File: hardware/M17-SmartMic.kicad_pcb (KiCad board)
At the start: 4 copper layers, 84.9 x 89.9 mm, 182 parts, among them IC1 LM4861M, J1 Kenwood-2.5, J10 UART, J11 Radio_Opt, J12 Speaker, J2 USB_C, J3 OLED, J4 CAT_TX, J5 Kenwood-3.5, J6 CAT_TX, J7 Radio, J8 +12V, J9 STLink, Q1 IRLML2060, Q2 BSS138, Q3 BSS138, Q4 IRLML2244, Q5 MMBT3904, SW1 Button Up, SW2 Button Down, SW3 Reset, SW4 Button Escape, SW5 Button Left, SW6 Button Enter, SW7 Button Right, SW8 Button Power, U1 MAX9814, U10 STM32F405RGTx, U11 TPS7A2033, U2 TP6841S6, U3 USBLC6-2, U6 MCP6002, U7 MCP6002, Y1 8 MHz

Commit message: Started new PCB layout
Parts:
- removed C10: 1n, pkl_dipol:C_0603
- removed R2: 22k, pkl_dipol:R_0603
- added C201: 10n, pkl_dipol:C_0603, F.Cu at (126.8, 121.5)
- added C202: 4.7n, pkl_dipol:C_0603, F.Cu at (116.6, 123.2)
- added C203: 100n, pkl_dipol:C_0603, F.Cu at (121.0, 121.8)
- added C513: 100n, pkl_dipol:C_0603, F.Cu at (151.5, 68.9)
- added C514: 100n, pkl_dipol:C_0603, F.Cu at (132.3, 68.6)
- added R201: 7.5k, pkl_dipol:R_0603, F.Cu at (123.0, 125.8)
- added R202: 4.7k, pkl_dipol:R_0603, F.Cu at (123.7, 123.2)
- added R69: 0, pkl_dipol:R_0603, F.Cu at (106.0, 134.5)
- added R70: 0, pkl_dipol:R_0603, F.Cu at (106.0, 136.8)
- added U201: MCP6002, Package_SO:SOIC-8_3.9x4.9mm_P1.27mm, F.Cu at (132.9, 123.1)
- added U503: MCP4551, Package_SO:MSOP-8_3x3mm_P0.65mm, F.Cu at (135.1, 71.5)
- added U504: MCP4551, Package_SO:MSOP-8_3x3mm_P0.65mm, F.Cu at (154.2, 70.7)
- IC1: value LM4861M -> LM4991xx
- RV2, RV3: footprint Potentiometer_SMD:Potentiometer_Bourns_3224W_Vertical -> Potentiometer_SMD:Potentiometer_Bourns_3224J_Horizontal
- moved Ref** 179.8 mm to (28.6, 40.9)
- moved Ref** 177.8 mm to (30.9, 25.3)
- moved REF** 172.6 mm to (25.7, 56.8)
- moved REF** 172.6 mm to (25.7, 55.9)
- moved J9 123.3 mm to (65.8, 84.5), turned to 180 degrees
- moved R50 122.7 mm to (69.2, 79.8), turned to 180 degrees
- moved R3 121.3 mm to (69.2, 81.2), turned to 180 degrees
- moved R4 119.9 mm to (69.2, 82.6), turned to 180 degrees
- moved Q1 114.8 mm to (106.4, 122.8), turned to 0 degrees
- moved C54 111.1 mm to (109.0, 122.8), turned to 90 degrees
- moved R49 108.2 mm to (111.1, 122.0), turned to 180 degrees
- moved R51 108.1 mm to (111.1, 123.5), turned to 0 degrees
- moved TP6 108.0 mm to (76.8, 120.2)
- moved J6 106.8 mm to (96.1, 109.8), turned to 90 degrees
- moved J4 104.6 mm to (97.7, 109.8), turned to 90 degrees
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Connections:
- net /Microcontroller/xUDN renamed /Connectors/xUDN
- net /Microcontroller/xUDP renamed /Connectors/xUDP
- net Net-(R41-Pad2) renamed /Baseband/BB_RX_A
- net Net-(R42-Pad1) renamed /Baseband/BB_RX_B
- net Net-(U6A-+) renamed /Baseband/BB_TX_W
- net Net-(U7A--) renamed /Baseband/BB_RX_W
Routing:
- net +5V: track 197.6 -> 20.9 mm, vias 6 -> 1
- net VDD: track 94.8 -> 0.00 mm, vias 19 -> 2
- net BTN_RIGHT: track 77.7 -> 0.00 mm, vias 2 -> 0
- net BTN_DOWN: track 76.7 -> 0.00 mm, vias 2 -> 0
- net BTN_LEFT: track 65.2 -> 0.00 mm, vias 2 -> 0
- net BTN_ENT: track 65.1 -> 0.00 mm, vias 2 -> 0
- net ~{BOOT0}: track 59.6 -> 0.00 mm, vias 2 -> 0
- net BTN_UP: track 59.0 -> 0.00 mm, vias 2 -> 0
- net LED-ERROR: track 50.4 -> 0.00 mm, vias 2 -> 0
- net LED-SYNC: track 50.0 -> 0.00 mm, vias 2 -> 0
- net LED-PTT: track 49.6 -> 0.00 mm, vias 2 -> 0
- net VIN: track 79.3 -> 31.6 mm
- net GPIO_POWER: track 47.7 -> 1.62 mm, vias 2 -> 1
- net NRST: track 45.1 -> 0.00 mm, vias 1 -> 0
- net OLED_SPI_MOSI: track 40.6 -> 0.00 mm, vias 1 -> 0
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- removed copper zone on B.Cu, net GND
- removed copper zone on F.Cu, net GND
- removed copper zone on In2.Cu, net GND
- removed copper zone on In1.Cu, net VDD
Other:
- board size 84.9 x 89.9 mm -> 100 x 80 mm
- board text added: "OHIS 8P8C"
- board text added: "TP_BBRX"
- board text added: "TP_BBTX"
- board text removed: "SPK_PRE"

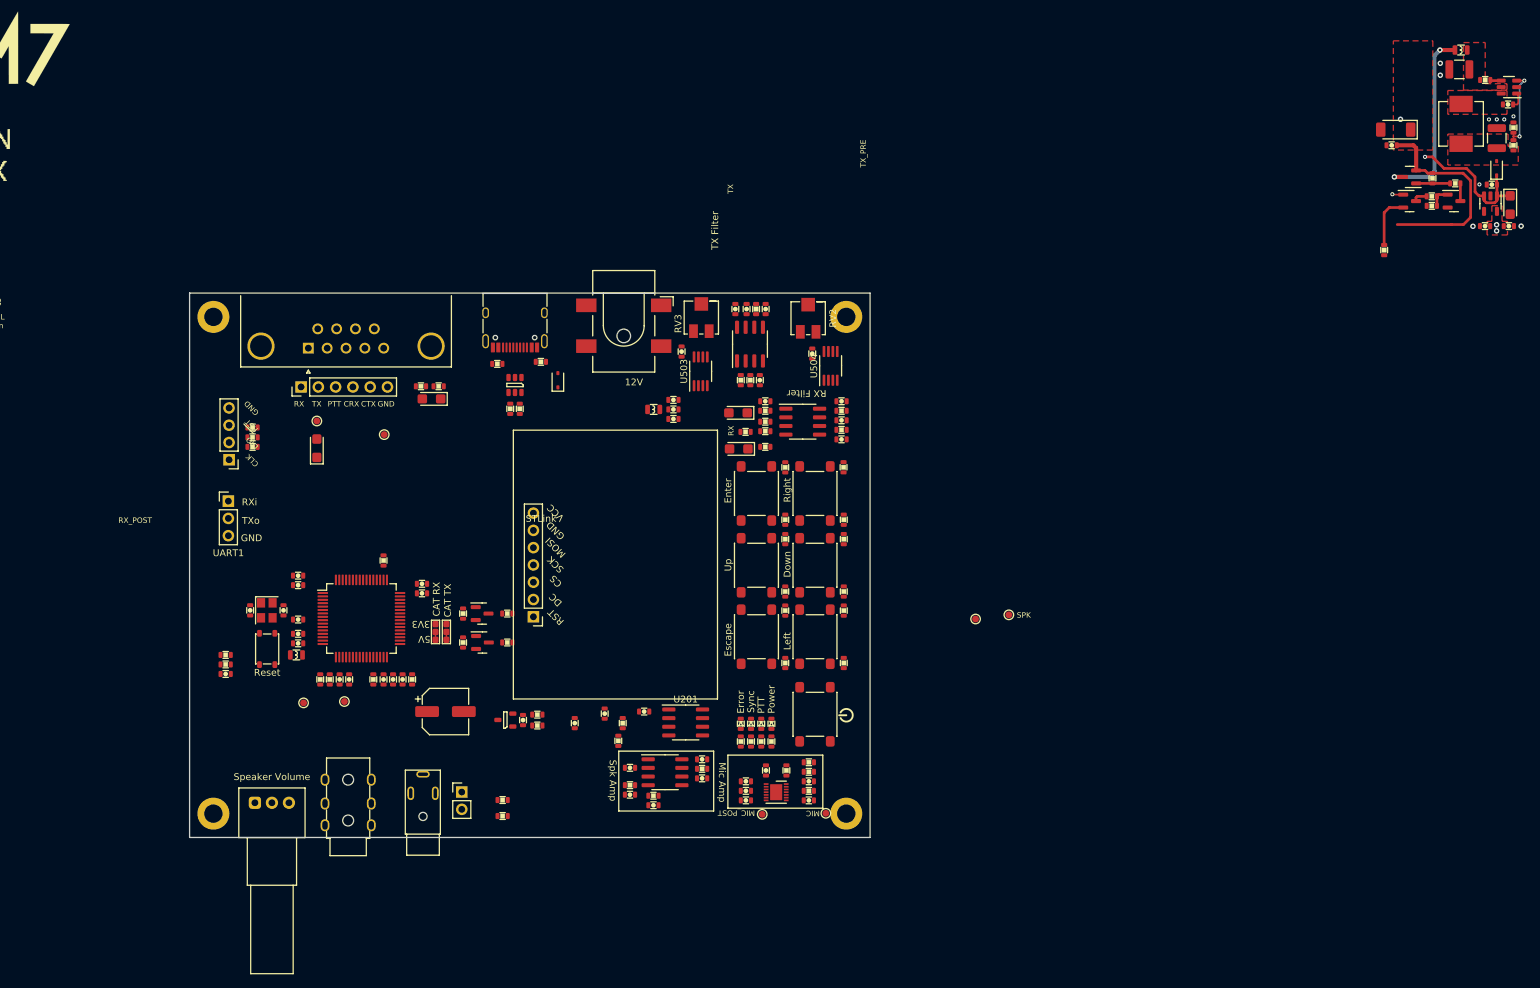
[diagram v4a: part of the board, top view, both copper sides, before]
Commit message: [WIP] PCB layout and routing
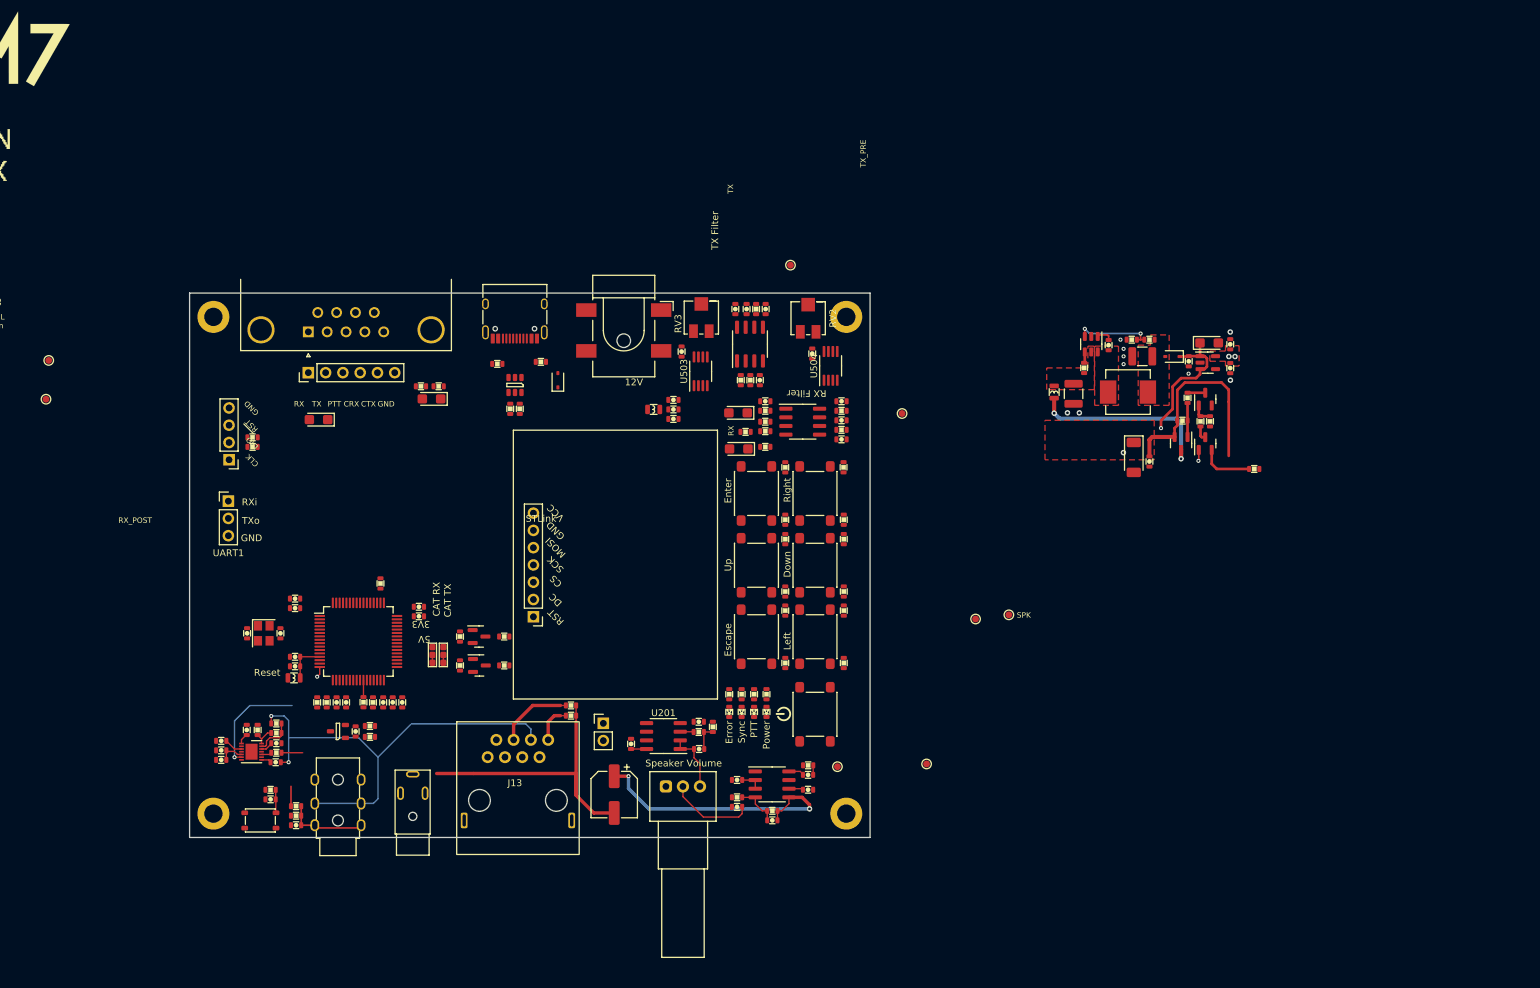
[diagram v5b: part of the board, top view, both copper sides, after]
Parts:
- added J13: KH-RJ45-58-8P8C, M17-SmartMic:KH-RJ45-58-8P8C, F.Cu at (108.2, 142.5)
- moved TP6 97.7 mm to (164.7, 77.7)
- moved TP5 91.7 mm to (148.3, 55.9)
- moved R1 78.6 mm to (72.8, 123.2), turned to 180 degrees
- moved C9 78.5 mm to (72.7, 128.9)
- moved C21 78.5 mm to (72.8, 126.2)
- moved R8 78.5 mm to (72.8, 127.5)
- moved R30 78.4 mm to (72.8, 124.7), turned to 0 degrees
- moved FB2 78.1 mm to (187.1, 74.5), turned to -90 degrees
- moved R23 77.9 mm to (70.0, 124.2)
- moved C29 77.3 mm to (64.7, 125.8)
- moved C46 77.3 mm to (64.7, 128.6)
- moved C47 77.3 mm to (64.7, 127.2)
- moved U1 77.3 mm to (69.1, 127.4)
- moved C12 76.5 mm to (68.4, 124.2)
- moved C62 74.1 mm to (189.9, 74.8), turned to -90 degrees
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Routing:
- net MIC: track 0.00 -> 67.5 mm, vias 0 -> 2
- net SPEAKER: track 0.14 -> 43.7 mm
- net Net-(IC1-VO1): track 0.00 -> 40.3 mm, vias 0 -> 2
- net AUDIO_MIC: track 0.00 -> 17.3 mm, vias 0 -> 2
- net Net-(C20-Pad1): track 0.00 -> 12.6 mm
- net Net-(C32-Pad1): track 0.00 -> 11.9 mm
- net Net-(J13-Pad4): track 0.00 -> 11.0 mm
- net Net-(U201A--): track 0.00 -> 9.16 mm
- net Net-(IC1--IN): track 0.00 -> 6.48 mm
- net VDDA: track 0.00 -> 5.97 mm
- net Net-(U1-MICBIAS): track 0.00 -> 5.73 mm
- net Net-(J13-Pad8): track 0.00 -> 5.53 mm
- net VDD: track 0.00 -> 3.87 mm
- net Net-(C201-Pad1): track 0.00 -> 3.72 mm
- net Net-(U1-TH): track 0.00 -> 3.28 mm
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- added copper zone on In1.Cu, net GND
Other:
- board text added: "Volume knob sticks out of the board by : 1.6mm (PCB thickness for enclosure) + 2mm (nut thickness) + 0.5mm (washer thickness) + 0.4mm (tolerance margin) = 4.5mm"
- board text removed: "MIC"
- board text removed: "MIC_POST"
- board text removed: "Mic Amp"
- board text removed: "OHIS 8P8C"
- board text removed: "Spk Amp"

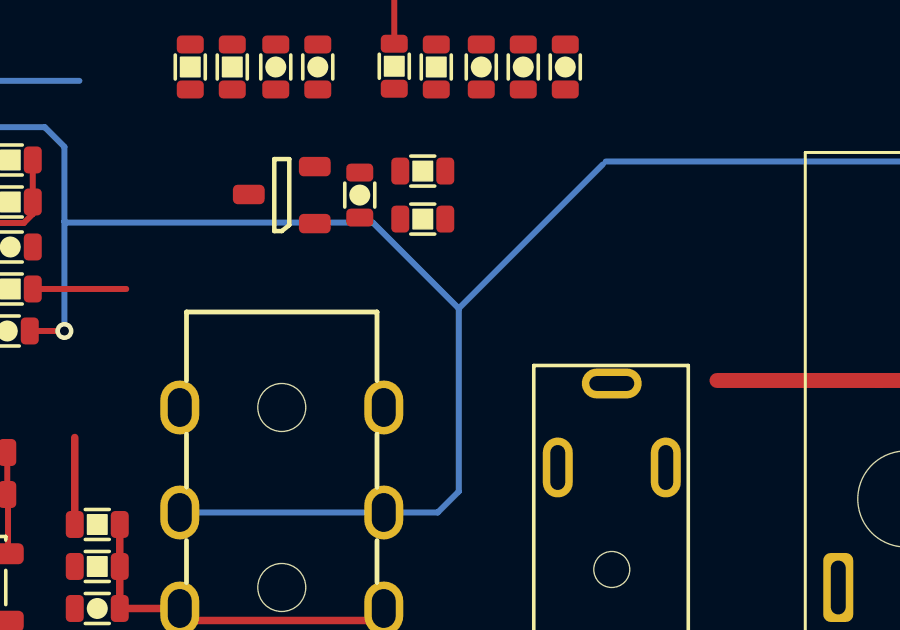
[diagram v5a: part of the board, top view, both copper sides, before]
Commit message: Switched to M17_kicad_library for custom symbols/footprints
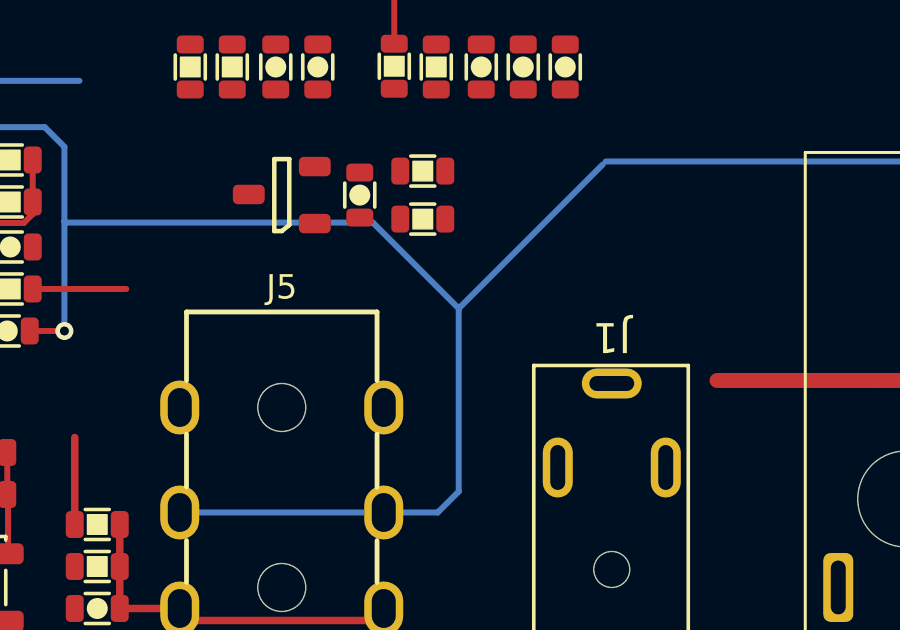
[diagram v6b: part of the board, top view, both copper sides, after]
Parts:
- J1: footprint M17-SmartMic:PJ-211A -> M17_connectors:PJ-211A
- J13: footprint M17-SmartMic:KH-RJ45-58-8P8C -> M17_connectors:KH-RJ45-58-8P8C
- J5: footprint M17-SmartMic:PJ-3136-B -> M17_connectors:PJ-3136-B
- U503: value MCP4551 -> MCP4551-103
- U504: value MCP4551 -> MCP455x
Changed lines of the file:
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@@
   (net 147 "Net-(J2-CC2)")
   (net 148 "Net-(J2-CC1)")
-  (footprint "M17-SmartMic:KH-RJ45-58-8P8C" (layer "F.Cu")
+  (footprint "M17_connectors:KH-RJ45-58-8P8C" (layer "F.Cu")
     (at 108.25 142.5)
     (property "LCSC Part #" "C2683360")
@@
       (net 45 "RADIO_TX") (pinfunction "1") (pintype "passive"))
   )
-  (footprint "M17-SmartMic:PJ-211A" (layer "F.Cu")
+  (footprint "M17_connectors:PJ-211A" (layer "F.Cu")
     (at 92.8 136.9 90)
     (property "LCSC Part #" "C480265")
@@
     (property "ki_keywords" "audio jack receptacle stereo headphones phones TRS connector")
     (attr through_hole)
-    (fp_text reference "J1" (at 7.75 0 180 unlocked) (layer "F.Fab")
+    (fp_text reference "J1" (at 7.75 0 180 unlocked) (layer "F.SilkS")
         (effects (font (size 1 1) (thickness 0.15)))
     )
@@
     (descr "SOIC, 8 Pin (JEDEC MS-012AA, https://www.analog.com/media/en/package-pcb-resources/package/pkg_pdf/soic_narrow-r/r_8.pdf), generated with kicad-footprint-generator ipc_gullwing_generator.py")
     (tags "SOIC SO")
-    (property "Description" "TEXAS INSTRUMENTS - LM4991xx - Audio Power Amplifier, 3 W, AB, 1 Channel, 2V to 5.5V, 8 Pins")
+    (property "LCSC Part #" "C2860134")
+    (property "MPN" "LM4991MA/NOPB")
     (property "Sheetfile" "Audio.kicad_sch")
     (property "Sheetname" "Audio & Filter")
     (property "ki_description" "TEXAS INSTRUMENTS - LM4991 - Audio Power Amplifier, 3 W, AB, 1 Channel, 2V to 5.5V, 8 Pins")
+    (property "ki_keywords" "Audio Amplifier shutdown")
     (attr smd)
     (fp_text reference "IC1" (at 0.035 -0.015) (layer "F.Fab")
@@
     (descr "MSOP, 8 Pin (https://www.jedec.org/system/files/docs/mo-187F.pdf variant AA), generated with kicad-footprint-generator ipc_gullwing_generator.py")
     (tags "MSOP SO")
+    (property "LCSC Part #" "C636116")
+    (property "MPN" "MCP4551-103E/MS")
     (property "Sheetfile" "baseband.kicad_sch")
     (property "Sheetname" "Baseband")
+    (property "ki_description" "7/8-Bit Single/Dual I2C Digital POT with Volatile Memory")
+    (property "ki_keywords" "digital potentiometer")
     (attr smd)
     (fp_text reference "U503" (at 0 -2.45 90) (layer "F.SilkS")
         (effects (font (size 1 1) (thickness 0.15)))
     )
-    (fp_text value "MCP4551" (at 0 2.45 90) (layer "F.Fab")
+    (fp_text value "MCP4551-103" (at 0 2.45 90) (layer "F.Fab")
         (effects (font (size 1 1) (thickness 0.15)))
     )
@@
     )
   )
-  (footprint "M17-SmartMic:PJ-3136-B" (layer "F.Cu")
+  (footprint "M17_connectors:PJ-3136-B" (layer "F.Cu")
     (at 81.8 140 90)
     (property "LCSC Part #" "C381131")
@@
     (property "ki_keywords" "audio jack receptacle stereo headphones phones TRS connector")
     (attr through_hole)
-    (fp_text reference "J5" (at 12.5095 0) (layer "F.Fab")
+    (fp_text reference "J5" (at 12.5095 0 180) (layer "F.SilkS")
         (effects (font (size 0.8128 0.8128) (thickness 0.1524)))
     )
@@
         (effects (font (size 0.8128 0.8128) (thickness 0.1524)))
     )
-    (fp_text user "${REFERENCE}" (at 12.5095 0) (layer "B.Fab")
+    (fp_text user "${REFERENCE}" (at 12.5095 0 180) (layer "B.SilkS")
         (effects (font (size 0.8128 0.8128) (thickness 0.1524)) (justify mirror))
     )
@@
     (descr "MSOP, 8 Pin (https://www.jedec.org/system/files/docs/mo-187F.pdf variant AA), generated with kicad-footprint-generator ipc_gullwing_generator.py")
     (tags "MSOP SO")
+    (property "LCSC Part #" "C636116")
+    (property "MPN" "MCP4551-103E/MS")
     (property "Sheetfile" "baseband.kicad_sch")
     (property "Sheetname" "Baseband")
+    (property "ki_description" "7/8-Bit Single/Dual I2C Digital POT with Volatile Memory")
+    (property "ki_keywords" "digital potentiometer")
     (attr smd)
     (fp_text reference "U504" (at 0 -2.45 90) (layer "F.SilkS")
         (effects (font (size 1 1) (thickness 0.15)))
     )
-    (fp_text value "MCP4551" (at 0 2.45 90) (layer "F.Fab")
+    (fp_text value "MCP455x" (at 0 2.45 90) (layer "F.Fab")
         (effects (font (size 1 1) (thickness 0.15)))
     )
@@
     (property "Sheetfile" "Microcontroller.kicad_sch")
     (property "Sheetname" "Microcontroller")
+    (property "ki_description" "40V 0.8A 800kHz Synchronous Step-Down Converter")
+    (property "ki_keywords" "buck converter step-down")
     (attr smd)
     (fp_text reference "U2" (at 0 -2.4 -270) (layer "F.Fab")

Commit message: Synchronized PCB and schematic
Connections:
- FB1 pad 1: VDDA -> VDD
- FB1 pad 2: VDD -> VDDA
- U10 pad 55: SPI1_SCK -> unconnected-(U10-PB3-Pad55)
- U10 pad 56: SPI1_MISO -> unconnected-(U10-PB4-Pad56)
- U10 pad 57: SPI1_MOSI -> unconnected-(U10-PB5-Pad57)
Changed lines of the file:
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@@
   (net 64 "BTN_RIGHT")
   (net 65 "GPIO_POWER")
-  (net 66 "SPI1_SCK")
+  (net 66 "unconnected-(U10-PB3-Pad55)")
   (net 67 "LED-PTT")
   (net 68 "LED-SYNC")
@@
   (net 111 "Net-(U2-EN)")
   (net 112 "VBAT")
-  (net 113 "SPI1_MISO")
-  (net 114 "SPI1_MOSI")
+  (net 113 "unconnected-(U10-PB4-Pad56)")
+  (net 114 "unconnected-(U10-PB5-Pad57)")
   (net 115 "Net-(R29-Pad1)")
   (net 116 "Net-(U2-FB)")
@@
       (stroke (width 0.1) (type solid)) (fill none) (layer "F.Fab"))
     (pad "1" smd roundrect (at -0.9 0 180) (size 0.7 1.4) (layers "F.Cu" "F.Paste" "F.Mask") (roundrect_rratio 0.25)
-      (net 6 "VDDA") (pintype "passive"))
-    (pad "2" smd roundrect (at 0.9 0 180) (size 0.7 1.4) (layers "F.Cu" "F.Paste" "F.Mask") (roundrect_rratio 0.25)
       (net 1 "VDD") (pintype "passive"))
+    (pad "2" smd roundrect (at 0.9 0 180) (size 0.7 1.4) (layers "F.Cu" "F.Paste" "F.Mask") (roundrect_rratio 0.25)
+      (net 6 "VDDA") (pintype "passive"))
     (model "${KISYS3DMOD}/Inductor_SMD.3dshapes/L_0805_2012Metric.wrl"
       (offset (xyz 0 0 0))
@@
       (net 78 "~{PTT_OUT}") (pinfunction "PD2") (pintype "bidirectional"))
     (pad "55" smd roundrect (at 0.75 -5.675) (size 0.3 1.55) (layers "F.Cu" "F.Paste" "F.Mask") (roundrect_rratio 0.25)
-      (net 66 "SPI1_SCK") (pinfunction "PB3") (pintype "bidirectional"))
+      (net 66 "unconnected-(U10-PB3-Pad55)") (pinfunction "PB3") (pintype "bidirectional+no_connect"))
     (pad "56" smd roundrect (at 0.25 -5.675) (size 0.3 1.55) (layers "F.Cu" "F.Paste" "F.Mask") (roundrect_rratio 0.25)
-      (net 113 "SPI1_MISO") (pinfunction "PB4") (pintype "bidirectional"))
+      (net 113 "unconnected-(U10-PB4-Pad56)") (pinfunction "PB4") (pintype "bidirectional+no_connect"))
     (pad "57" smd roundrect (at -0.25 -5.675) (size 0.3 1.55) (layers "F.Cu" "F.Paste" "F.Mask") (roundrect_rratio 0.25)
-      (net 114 "SPI1_MOSI") (pinfunction "PB5") (pintype "bidirectional"))
+      (net 114 "unconnected-(U10-PB5-Pad57)") (pinfunction "PB5") (pintype "bidirectional+no_connect"))
     (pad "58" smd roundrect (at -0.75 -5.675) (size 0.3 1.55) (layers "F.Cu" "F.Paste" "F.Mask") (roundrect_rratio 0.25)
       (net 99 "I2C_SCL") (pinfunction "PB6") (pintype "bidirectional"))
